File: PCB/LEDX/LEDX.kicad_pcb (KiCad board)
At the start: 2 copper layers, 70 x 70 mm, 23 parts, among them J2 Conn_01x03, J3 TC2030-USB-NL-DS, U1 ICS43434_MEMS_Mic, U2 ESP32-S3-MINI-1, U5 MD8942

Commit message: Started
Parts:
- added C5: 100nF, RevK:C_0402, F.Cu at (111.5, 95.5)
- added U3: 78L05, RevK:SOT-23, F.Cu at (112.4, 94.0)
- C4, D1, D2: moved to B.Cu
- moved D2 13.4 mm to (106.0, 107.0)
- moved C4 10.9 mm to (103.0, 107.0), turned to 180 degrees
- moved C1 2.24 mm to (110.0, 97.0)
- moved C2 2.00 mm to (109.5, 98.0), turned to 180 degrees
- moved C3 1.50 mm to (112.0, 97.0)
- moved D1 1.50 mm to (111.5, 93.5)
- moved R1 1.00 mm to (111.5, 98.0)
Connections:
- net LED1 renamed LED
- D1 pad 1: unconnected-(D1-O-Pad1) -> Net-(D1-O)
- D1 pad 2: +3.3V -> Net-(D1-+)
- D2 pad 2: LED2 -> Net-(D1-O)
- J2 pad 2: LED2 -> Net-(D1-O)
- U2 pad 5: LED2 -> unconnected-(U2-GPIO1-Pad5)
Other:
- board text added: "4"
- board text added: "Made in China"
- board text removed: "1"

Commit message: Tracked
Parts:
- C3, R1: moved to B.Cu
- moved C3 18.7 mm to (93.7, 93.1)
- moved R1 16.7 mm to (95.5, 93.1), turned to 180 degrees
- moved D2 12.2 mm to (93.8, 106.9)
- moved C4 2.90 mm to (105.9, 107.0), turned to 0 degrees
- moved C5 2.19 mm to (112.4, 97.5)
- moved C1 1.58 mm to (111.5, 97.5), turned to 90 degrees
- moved D1 1.54 mm to (113.0, 93.5), turned to 0 degrees
- moved C2 1.21 mm to (110.6, 97.5), turned to 90 degrees
- moved J3 0.07 mm to (110.9, 96.9)
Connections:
- U2 pad 16: WS -> unconnected-(U2-GPIO12-Pad16)
- U2 pad 17: SD -> unconnected-(U2-GPIO13-Pad17)
- U2 pad 18: +3.3V -> unconnected-(U2-GPIO14-Pad18)
- U2 pad 19: SCK -> unconnected-(U2-GPIO15-Pad19)
- U2 pad 25: unconnected-(U2-GPIO21-Pad25) -> WS
- U2 pad 28: unconnected-(U2-GPIO33-Pad28) -> SD
- U2 pad 29: unconnected-(U2-GPIO34-Pad29) -> +3.3V
- U2 pad 30: unconnected-(U2-GPIO48-Pad30) -> SCK
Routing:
- net DC: track 0.00 -> 53.5 mm, vias 0 -> 5
- net +3.3V: track 0.75 -> 47.2 mm, vias 0 -> 3
- net Net-(D1-O): track 0.00 -> 36.7 mm, vias 0 -> 2
- net LED: track 0.00 -> 27.6 mm, vias 0 -> 1
- net D+: track 0.00 -> 13.2 mm, vias 0 -> 1
- net D-: track 0.00 -> 12.7 mm, vias 0 -> 1
- net GND: track 0.00 -> 7.61 mm, vias 0 -> 15
- net Net-(D1-+): track 0.00 -> 5.94 mm, vias 0 -> 1
- net WS: track 0.00 -> 4.68 mm
- net Net-(U2-EN): track 0.00 -> 3.36 mm, vias 0 -> 1
- net SD: track 0.00 -> 3.09 mm
- net SCK: track 0.00 -> 1.89 mm
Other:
- board text added: "led.revk.uk"

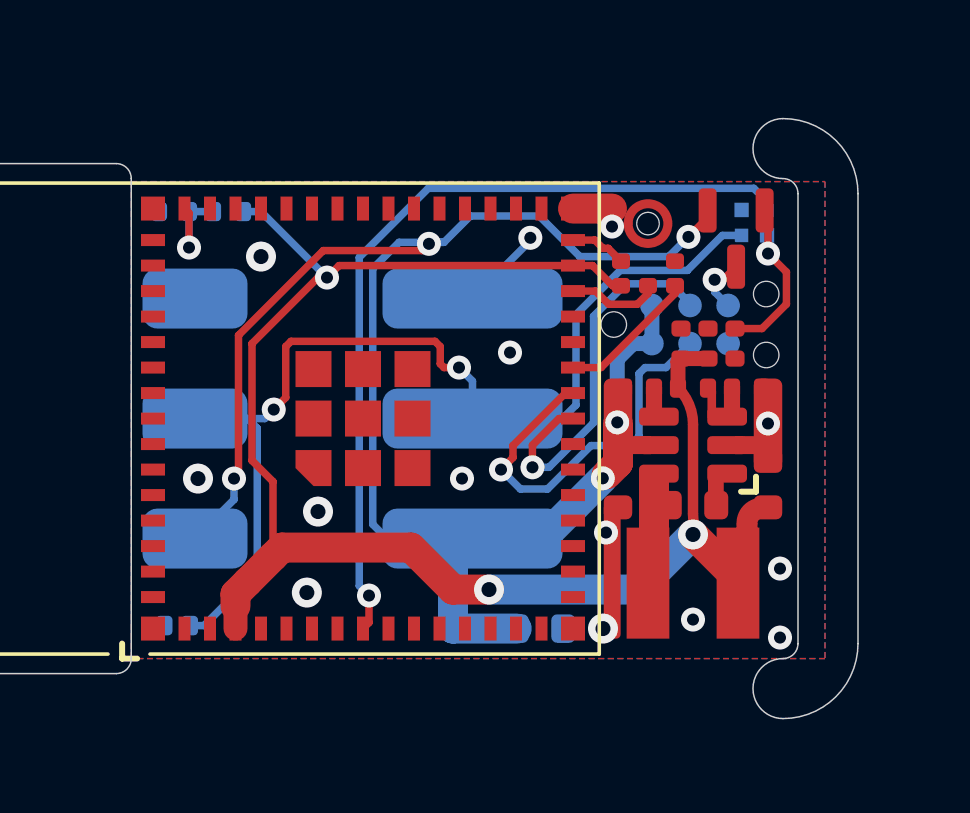
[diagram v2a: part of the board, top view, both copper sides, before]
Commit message: Not level convert as fixes to RGB mode
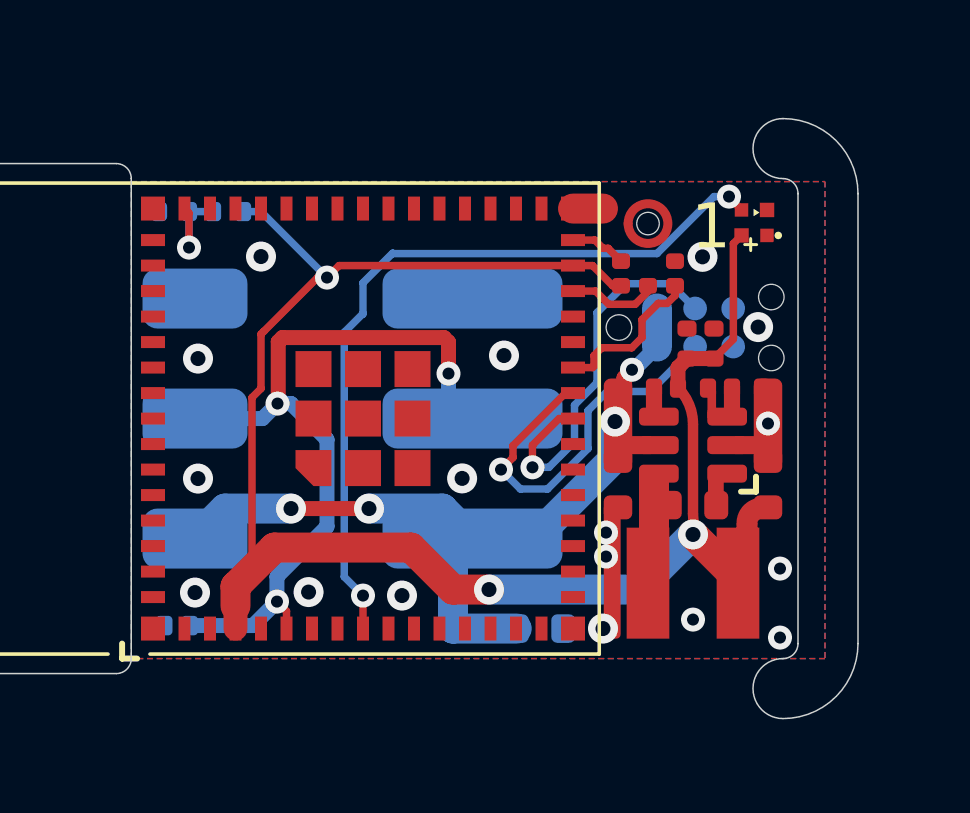
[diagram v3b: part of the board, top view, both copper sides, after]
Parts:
- removed C5: 100nF, RevK:C_0402
- removed U3: 78L05, RevK:SOT-23
- D1: moved to F.Cu
- moved C1 0.20 mm to (111.7, 97.5)
- moved C2 0.20 mm to (110.8, 97.5)
- moved J3 0.20 mm to (111.1, 97.0)
- turned D1 to 180 degrees
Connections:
- net LED renamed LED2
- D1 pad 1: Net-(D1-O) -> unconnected-(D1-O-Pad1)
- D1 pad 2: Net-(D1-+) -> +3.3V
- D2 pad 2: Net-(D1-O) -> LED1
- J2 pad 2: Net-(D1-O) -> LED1
- U2 pad 5: unconnected-(U2-GPIO1-Pad5) -> LED1
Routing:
- net Net-(D1-O): track 36.7 -> 0.00 mm, vias 2 -> 0
- net DC: track 53.5 -> 25.7 mm, vias 5 -> 4
- net LED1: track 0.00 -> 26.2 mm, vias 0 -> 3
- net GND: track 7.61 -> 1.00 mm, vias 15 -> 17
- net Net-(D1-+): track 5.94 -> 0.00 mm, vias 1 -> 0
- net +3.3V: track 47.2 -> 52.8 mm
- net LED2: track 27.6 -> 26.1 mm, vias 1 -> 2
- net WS: track 4.68 -> 5.28 mm
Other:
- board text added: "1"
- board text added: "5V- 35V"
- board text added: "C48 C33 W21"
- board text removed: "C15 D13 W12"

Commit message: Tidy tracks
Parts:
- moved C1 0.70 mm to (111.0, 97.5)
- moved C2 0.70 mm to (110.1, 97.5)
- moved C4 0.60 mm to (105.3, 107.0)
- moved D1 0.54 mm to (112.5, 93.5)
- moved D2 0.51 mm to (94.3, 107.0)
- moved J3 0.30 mm to (110.8, 97.0)
- moved C6 0.20 mm to (108.3, 102.2)
- moved C7 0.20 mm to (113.3, 102.2)
- moved C8 0.20 mm to (110.8, 102.9)
- moved L2 0.20 mm to (110.8, 105.5)
- moved R10 0.20 mm to (112.6, 99.0)
- moved R11 0.20 mm to (109.0, 99.0)
- moved R9 0.20 mm to (110.8, 99.0)
- moved U5 0.20 mm to (110.8, 100.9)
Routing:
- net DC: track 25.7 -> 25.0 mm
- net +3.3V: track 52.8 -> 53.4 mm
- net GND: vias 17 -> 12
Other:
- board text added: "A"
- board text added: "B"

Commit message: Pads
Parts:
- added P1: Square, RevK:PAD-2mm, B.Cu at (112.5, 103.0)
- added P2: Square, RevK:PAD-2mm, B.Cu at (112.5, 94.0)
- added P3: Square, RevK:PAD-2mm, B.Cu at (112.5, 100.0)
- added P4: Square, RevK:PAD-2mm, B.Cu at (112.5, 106.0)
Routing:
- net DC: track 25.0 -> 32.1 mm
- net D+: track 12.8 -> 15.9 mm
- net D-: track 12.6 -> 15.6 mm
- net LED2: track 26.1 -> 25.4 mm
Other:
- board text added: "0"
- board text added: "5"
- board text added: "5-35V"
- board text removed: "5V- 35V"
- board text removed: "A"
- board text removed: "B"
